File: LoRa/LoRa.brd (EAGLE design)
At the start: 59.4 x 27.9 mm, 33 parts, among them J1 UP2-AH-1-TH, U1 STM32L053C8T6, U2 RFM69HCW, U5 LM3671MF-3.3/NOPB, X1 uFL/SMA, Y1 ECS-80-S-4X

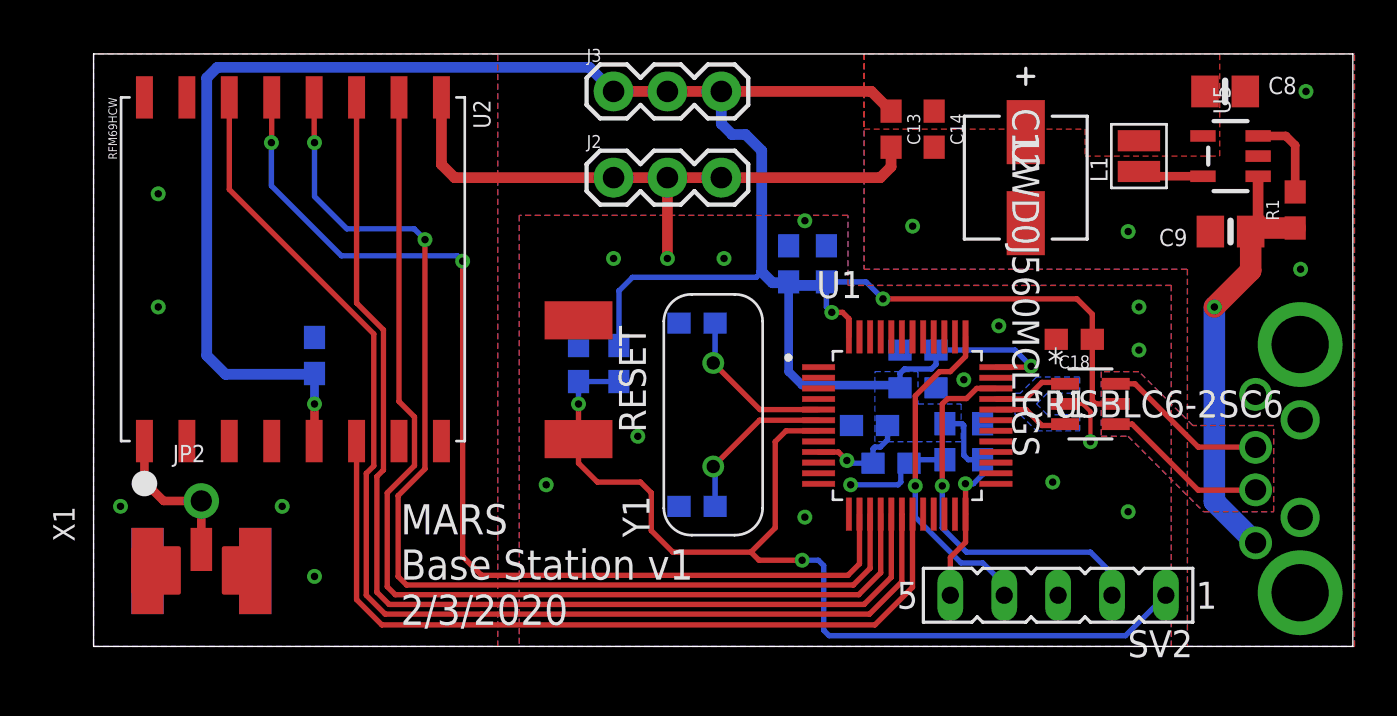
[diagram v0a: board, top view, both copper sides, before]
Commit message: LDO changes
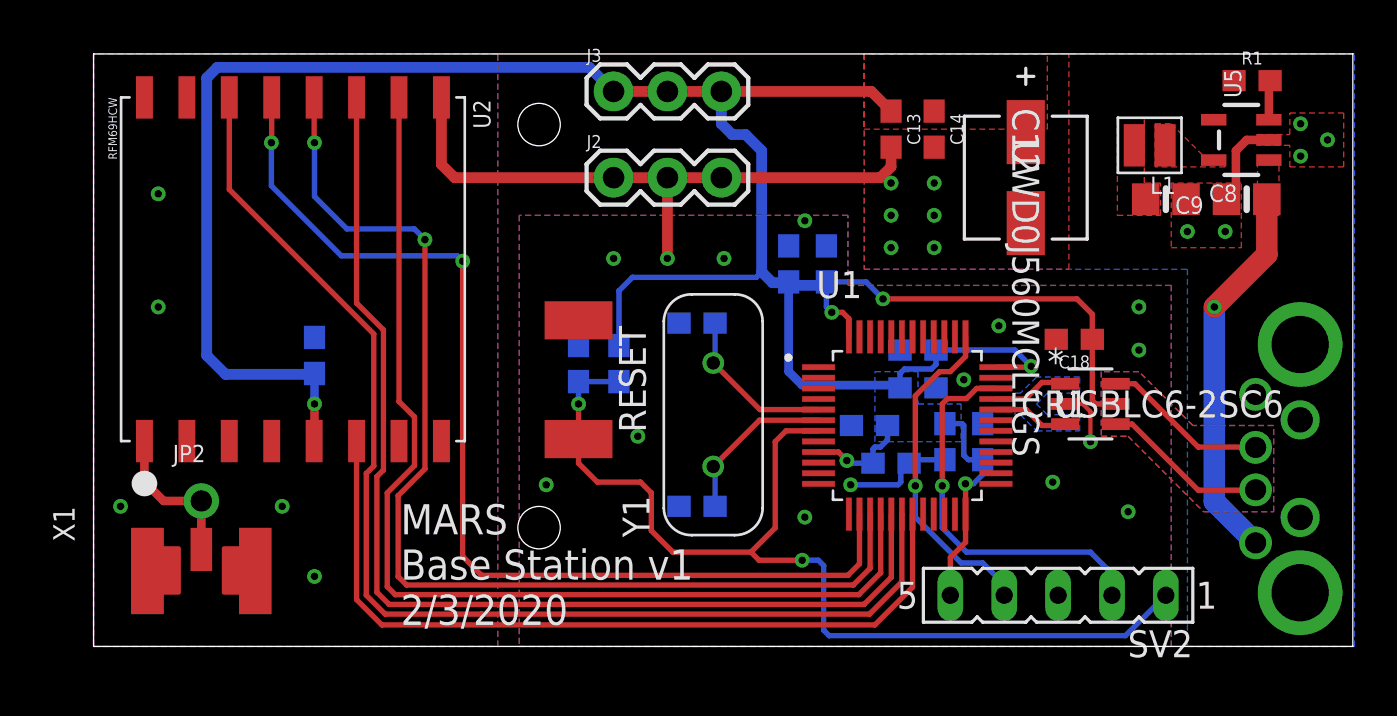
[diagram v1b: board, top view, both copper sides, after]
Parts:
- moved R1 6.43 mm to (54.6, 26.7), turned to 0 degrees
- moved C8 5.80 mm to (50.5, 21.1)
- moved C9 1.70 mm to (54.4, 21.1)
- moved U5 0.92 mm to (54.1, 23.9)
- moved L1 0.72 mm to (49.8, 23.6), turned to 180 degrees
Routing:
- net GND: track 37.5 -> 41.7 mm, vias 24 -> 31
- net 5V: track 21.4 -> 18.0 mm
- net N$2: track 3.11 -> 0.00 mm
- net EN: track 4.13 -> 1.87 mm
- added copper zone on layer 1, net 5V
- added copper zone on layer 1, net N$2
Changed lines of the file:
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@@
 <setting verticaltext="up"/>
 </settings>
-<grid distance="10" unitdist="mil" unit="mil" style="lines" multiple="1" display="yes" altdistance="5" altunitdist="mil" altunit="mil"/>
+<grid distance="0.1" unitdist="mm" unit="mm" style="lines" multiple="1" display="yes" altdistance="5" altunitdist="mil" altunit="mil"/>
 <layers>
 <layer number="1" name="Top" color="4" fill="1" visible="yes" active="yes"/>
@@
 <layer number="43" name="vRestrict" color="2" fill="10" visible="yes" active="yes"/>
 <layer number="44" name="Drills" color="7" fill="1" visible="no" active="yes"/>
-<layer number="45" name="Holes" color="7" fill="1" visible="no" active="yes"/>
+<layer number="45" name="Holes" color="7" fill="1" visible="yes" active="yes"/>
 <layer number="46" name="Milling" color="3" fill="1" visible="no" active="yes"/>
 <layer number="47" name="Measures" color="7" fill="1" visible="no" active="yes"/>
@@
 Base Station v1
 2/3/2020</text>
+<hole x="21" y="24.6" drill="2"/>
+<hole x="21" y="5.6" drill="2"/>
 </plain>
 <attributes>
@@
 <attribute name="OC_NEWARK" value="unknown" x="45.466" y="2.413" size="1.778" layer="27" rot="R180" display="off"/>
 </element>
-<element name="U5" library="microbuilder" package="SOT23-5" value="LM3671MF-3.3/NOPB" x="53.594" y="23.114" rot="R90"/>
-<element name="L1" library="microbuilder" package="INDUCTOR_TAIYOYUDEN_NRH2412T" value="2.2uH/NRH2412T2R2MNGH" x="49.276" y="23.114" rot="R90"/>
-<element name="C8" library="microbuilder" package="0805-NO" value="22uF" x="53.34" y="26.162"/>
-<element name="C9" library="microbuilder" package="0805-NO" value="10uF" x="53.594" y="19.558" rot="R180"/>
-<element name="R1" library="SparkFun-Resistors" library_urn="urn:adsk.eagle:library:532" package="0603" package3d_urn="urn:adsk.eagle:package:39650/1" value="100k" x="56.642" y="20.574" rot="R90">
-<attribute name="PROD_ID" value="RES-07828" x="56.642" y="20.574" size="1.778" layer="27" rot="R90" display="off"/>
+<element name="U5" library="microbuilder" package="SOT23-5" value="LM3671MF-3.3/NOPB" x="54.102" y="23.876" rot="R90"/>
+<element name="L1" library="microbuilder" package="INDUCTOR_TAIYOYUDEN_NRH2412T" value="2.2uH/NRH2412T2R2MNGH" x="49.784" y="23.622" rot="R180"/>
+<element name="C8" library="microbuilder" package="0805-NO" value="22uF" x="50.546" y="21.082"/>
+<element name="C9" library="microbuilder" package="0805-NO" value="10uF" x="54.356" y="21.082" rot="R180"/>
+<element name="R1" library="SparkFun-Resistors" library_urn="urn:adsk.eagle:library:532" package="0603" package3d_urn="urn:adsk.eagle:package:39650/1" value="100k" x="54.61" y="26.67">
+<attribute name="PROD_ID" value="RES-07828" x="54.61" y="26.67" size="1.778" layer="27" display="off"/>
 </element>
 <element name="C10" library="SparkFun-Capacitors" library_urn="urn:adsk.eagle:library:510" package="0603" package3d_urn="urn:adsk.eagle:package:37414/1" value="20pF" x="28.448" y="6.604" rot="MR0">
@@
 <contactref element="C13" pad="2"/>
 <contactref element="C14" pad="2"/>
-<polygon width="0.2032" layer="1" rank="4">
-<vertex x="36.322" y="27.94"/>
-<vertex x="36.322" y="17.78"/>
-<vertex x="51.562" y="17.78"/>
-<vertex x="51.562" y="0"/>
-<vertex x="59.436" y="0"/>
-<vertex x="59.436" y="27.94"/>
-</polygon>
 <contactref element="C15" pad="2"/>
 <contactref element="C16" pad="2"/>
@@
 <via x="3.048" y="21.336" extent="1-16" drill="0.35"/>
 <via x="3.048" y="16.002" extent="1-16" drill="0.35"/>
-<via x="38.608" y="19.812" extent="1-16" drill="0.35"/>
-<via x="48.768" y="19.558" extent="1-16" drill="0.35"/>
-<via x="57.15" y="26.162" extent="1-16" drill="0.35"/>
-<via x="56.896" y="17.78" extent="1-16" drill="0.35"/>
+<via x="37.592" y="20.32" extent="1-16" drill="0.35"/>
 <via x="48.768" y="6.35" extent="1-16" drill="0.35"/>
 <via x="33.528" y="6.096" extent="1-16" drill="0.35"/>
+<polygon width="0.2032" layer="1" rank="4">
+<vertex x="36.322" y="27.94"/>
+<vertex x="36.322" y="17.78"/>
+<vertex x="45.974" y="17.78"/>
+<vertex x="45.974" y="27.94"/>
+</polygon>
+<via x="37.592" y="21.844" extent="1-16" drill="0.35"/>
+<via x="39.624" y="21.844" extent="1-16" drill="0.35"/>
+<polygon width="0.2032" layer="1" thermals="no">
+<vertex x="50.8" y="21.844"/>
+<vertex x="50.8" y="18.796"/>
+<vertex x="54.102" y="18.796"/>
+<vertex x="54.102" y="21.844"/>
+</polygon>
+<via x="51.562" y="19.558" extent="1-16" drill="0.35"/>
+<via x="53.34" y="19.558" extent="1-16" drill="0.35"/>
+<wire x1="55.4021" y1="23.876" x2="54.356" y2="23.876" width="0.4064" layer="1"/>
+<wire x1="53.848" y1="21.524" x2="53.406" y2="21.082" width="0.4064" layer="1"/>
+<wire x1="54.356" y1="23.876" x2="53.848" y2="23.368" width="0.4064" layer="1"/>
+<wire x1="53.848" y1="23.368" x2="53.848" y2="21.524" width="0.4064" layer="1"/>
+<polygon width="0.2032" layer="1" thermals="no">
+<vertex x="54.864" y="24.13"/>
+<vertex x="56.388" y="24.13"/>
+<vertex x="56.388" y="25.146"/>
+<vertex x="58.928" y="25.146"/>
+<vertex x="58.928" y="22.606"/>
+<vertex x="56.388" y="22.606"/>
+<vertex x="56.388" y="23.622"/>
+<vertex x="54.864" y="23.622"/>
+</polygon>
+<via x="56.896" y="24.638" extent="1-16" drill="0.35"/>
+<via x="58.166" y="23.876" extent="1-16" drill="0.35"/>
+<via x="56.896" y="23.114" extent="1-16" drill="0.35"/>
+<via x="37.592" y="18.796" extent="1-16" drill="0.35"/>
+<via x="39.624" y="18.796" extent="1-16" drill="0.35"/>
+<via x="39.624" y="20.32" extent="1-16" drill="0.35"/>
 </signal>
 <signal name="3.3V">
@@
 <contactref element="C13" pad="1"/>
 <contactref element="C14" pad="1"/>
-<wire x1="49.501" y1="24.064" x2="49.276" y2="23.839" width="0.4064" layer="1"/>
-<polygon width="0.2032" layer="1">
-<vertex x="36.322" y="27.94"/>
-<vertex x="36.322" y="24.384"/>
-<vertex x="46.736" y="24.384"/>
-<vertex x="46.736" y="23.114"/>
-<vertex x="53.086" y="23.114"/>
-<vertex x="53.086" y="27.94"/>
-</polygon>
 <contactref element="C15" pad="1"/>
 <contactref element="C16" pad="1"/>
@@
 <wire x1="47.078" y1="15.66" x2="47.078" y2="14.478" width="0.254" layer="1"/>
 <wire x1="46.355" y1="16.383" x2="47.078" y2="15.66" width="0.254" layer="1"/>
+<polygon width="0.2032" layer="1" thermals="no">
+<vertex x="36.322" y="27.94"/>
+<vertex x="36.322" y="24.384"/>
+<vertex x="44.958" y="24.384"/>
+<vertex x="44.958" y="27.94"/>
+</polygon>
+<polygon width="0.2032" layer="1" thermals="no">
+<vertex x="48.26" y="24.892"/>
+<vertex x="48.26" y="20.32"/>
+<vertex x="50.292" y="20.32"/>
+<vertex x="50.292" y="21.844"/>
+<vertex x="49.53" y="21.844"/>
+<vertex x="49.53" y="24.892"/>
+</polygon>
+<wire x1="49.059" y1="23.622" x2="52.8019" y2="24.826" width="0" layer="19" extent="1-1"/>
+<wire x1="43.942" y1="24.2443" x2="49.059" y2="23.622" width="0" layer="19" extent="1-1"/>
 </signal>
 <signal name="RST">
@@
 <contactref element="C9" pad="1"/>
 <contactref element="R1" pad="1"/>
-<wire x1="54.8941" y1="22.164" x2="54.8941" y2="19.558" width="0.508" layer="1"/>
-<wire x1="54.8941" y1="19.558" x2="54.544" y2="19.558" width="0.508" layer="1"/>
-<wire x1="54.544" y1="19.558" x2="54.544" y2="19.724" width="1.016" layer="1"/>
-<wire x1="54.544" y1="19.724" x2="56.642" y2="19.724" width="1.016" layer="1"/>
 <wire x1="54.776" y1="4.882" x2="52.832" y2="6.826" width="1.016" layer="16"/>
 <wire x1="52.832" y1="6.826" x2="52.832" y2="16.002" width="1.016" layer="16"/>
 <via x="52.832" y="16.002" extent="1-16" drill="0.35"/>
-<wire x1="52.832" y1="16.002" x2="54.544" y2="17.714" width="1.016" layer="1"/>
-<wire x1="54.544" y1="17.714" x2="54.544" y2="19.558" width="1.016" layer="1"/>
+<polygon width="0.2032" layer="1" thermals="no">
+<vertex x="54.864" y="20.32"/>
+<vertex x="54.864" y="23.114"/>
+<vertex x="55.88" y="23.114"/>
+<vertex x="55.88" y="20.32"/>
+</polygon>
+<wire x1="55.306" y1="21.082" x2="55.306" y2="18.476" width="1.016" layer="1"/>
+<wire x1="55.306" y1="18.476" x2="52.832" y2="16.002" width="1.016" layer="1"/>
+<wire x1="55.4021" y1="22.926" x2="53.76" y2="26.67" width="0" layer="19" extent="1-1"/>
 </signal>
 <signal name="SPI1_SCK">
@@
 <contactref element="L1" pad="1"/>
 <contactref element="U5" pad="5"/>
-<wire x1="52.2939" y1="22.164" x2="49.501" y2="22.164" width="0.4064" layer="1"/>
-<wire x1="49.501" y1="22.164" x2="49.276" y2="22.389" width="0.4064" layer="1"/>
+<polygon width="0.2032" layer="1" thermals="no">
+<vertex x="53.34" y="22.606"/>
+<vertex x="50.038" y="22.606"/>
+<vertex x="50.038" y="24.638"/>
+<vertex x="50.8" y="24.638"/>
+<vertex x="52.324" y="23.114"/>
+<vertex x="53.34" y="23.114"/>
+</polygon>
 </signal>
 <signal name="EN">
 <contactref element="U5" pad="3"/>
 <contactref element="R1" pad="2"/>
-<wire x1="54.8941" y1="24.064" x2="56.2" y2="24.064" width="0.4064" layer="1"/>
-<wire x1="56.2" y1="24.064" x2="56.642" y2="23.622" width="0.4064" layer="1"/>
-<wire x1="56.642" y1="23.622" x2="56.642" y2="21.424" width="0.4064" layer="1"/>
+<wire x1="55.4021" y1="24.826" x2="55.4021" y2="26.6121" width="0.4064" layer="1"/>
+<wire x1="55.4021" y1="26.6121" x2="55.46" y2="26.67" width="0.4064" layer="1"/>
 </signal>
 <signal name="OSC_OUT">

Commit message: This board is a work of art
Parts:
- moved R1 1.68 mm to (56.3, 26.6), turned to 180 degrees
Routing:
- net 3.3V: track 134.7 -> 144.9 mm
- net 5V: track 18.0 -> 28.1 mm
- net GND: vias 31 -> 32
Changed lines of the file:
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@@
 <setting verticaltext="up"/>
 </settings>
-<grid distance="0.1" unitdist="mm" unit="mm" style="lines" multiple="1" display="yes" altdistance="5" altunitdist="mil" altunit="mil"/>
+<grid distance="10" unitdist="mil" unit="mil" style="lines" multiple="1" display="yes" altdistance="5" altunitdist="mil" altunit="mil"/>
 <layers>
 <layer number="1" name="Top" color="4" fill="1" visible="yes" active="yes"/>
@@
 <element name="C8" library="microbuilder" package="0805-NO" value="22uF" x="50.546" y="21.082"/>
 <element name="C9" library="microbuilder" package="0805-NO" value="10uF" x="54.356" y="21.082" rot="R180"/>
-<element name="R1" library="SparkFun-Resistors" library_urn="urn:adsk.eagle:library:532" package="0603" package3d_urn="urn:adsk.eagle:package:39650/1" value="100k" x="54.61" y="26.67">
-<attribute name="PROD_ID" value="RES-07828" x="54.61" y="26.67" size="1.778" layer="27" display="off"/>
+<element name="R1" library="SparkFun-Resistors" library_urn="urn:adsk.eagle:library:532" package="0603" package3d_urn="urn:adsk.eagle:package:39650/1" value="100k" x="56.29" y="26.63" rot="R180">
+<attribute name="PROD_ID" value="RES-07828" x="56.29" y="26.63" size="1.778" layer="27" rot="R180" display="off"/>
 </element>
 <element name="C10" library="SparkFun-Capacitors" library_urn="urn:adsk.eagle:library:510" package="0603" package3d_urn="urn:adsk.eagle:package:37414/1" value="20pF" x="28.448" y="6.604" rot="MR0">
@@
 <vertex x="36.322" y="17.78"/>
 <vertex x="51.562" y="17.78"/>
-<vertex x="51.562" y="0"/>
-<vertex x="59.436" y="0"/>
+<vertex x="51.562" y="10.668"/>
+<vertex x="59.436" y="10.668"/>
 <vertex x="59.436" y="27.94"/>
 <vertex x="36.322" y="27.94"/>
@@
 <vertex x="54.102" y="21.844"/>
 </polygon>
-<via x="51.562" y="19.558" extent="1-16" drill="0.35"/>
-<via x="53.34" y="19.558" extent="1-16" drill="0.35"/>
+<via x="51.181" y="19.558" extent="1-16" drill="0.35"/>
+<via x="53.721" y="19.558" extent="1-16" drill="0.35"/>
 <wire x1="55.4021" y1="23.876" x2="54.356" y2="23.876" width="0.4064" layer="1"/>
 <wire x1="53.848" y1="21.524" x2="53.406" y2="21.082" width="0.4064" layer="1"/>
@@
 <vertex x="56.388" y="24.13"/>
 <vertex x="56.388" y="25.146"/>
-<vertex x="58.928" y="25.146"/>
-<vertex x="58.928" y="22.606"/>
+<vertex x="58.293" y="25.146"/>
+<vertex x="58.293" y="22.606"/>
 <vertex x="56.388" y="22.606"/>
 <vertex x="56.388" y="23.622"/>
@@
 </polygon>
 <via x="56.896" y="24.638" extent="1-16" drill="0.35"/>
-<via x="58.166" y="23.876" extent="1-16" drill="0.35"/>
+<via x="57.785" y="23.876" extent="1-16" drill="0.35"/>
 <via x="56.896" y="23.114" extent="1-16" drill="0.35"/>
 <via x="37.592" y="18.796" extent="1-16" drill="0.35"/>
 <via x="39.624" y="18.796" extent="1-16" drill="0.35"/>
 <via x="39.624" y="20.32" extent="1-16" drill="0.35"/>
+<via x="52.451" y="19.558" extent="1-16" drill="0.35"/>
 </signal>
 <signal name="3.3V">
@@
 <vertex x="49.53" y="24.892"/>
 </polygon>
+<wire x1="49.596" y1="21.082" x2="47.7393" y2="21.082" width="1.016" layer="1"/>
+<wire x1="47.7393" y1="21.082" x2="47.2313" y2="21.59" width="1.016" layer="1"/>
+<wire x1="47.2313" y1="25.0450875" x2="46.8890875" y2="25.3873" width="1.016" layer="1"/>
+<wire x1="44.6525125" y1="25.3873" x2="44.3103" y2="25.0450875" width="1.016" layer="1"/>
+<wire x1="47.2313" y1="21.59" x2="47.2313" y2="25.0450875" width="1.016" layer="1"/>
+<wire x1="46.8890875" y1="25.3873" x2="44.6525125" y2="25.3873" width="1.016" layer="1"/>
+<wire x1="44.3103" y1="25.0450875" x2="44.3103" y2="24.6126" width="1.016" layer="1"/>
+<wire x1="44.3103" y1="24.6126" x2="43.942" y2="24.2443" width="1.016" layer="1"/>
 <wire x1="49.059" y1="23.622" x2="52.8019" y2="24.826" width="0" layer="19" extent="1-1"/>
-<wire x1="43.942" y1="24.2443" x2="49.059" y2="23.622" width="0" layer="19" extent="1-1"/>
 </signal>
 <signal name="RST">
@@
 <wire x1="55.306" y1="21.082" x2="55.306" y2="18.476" width="1.016" layer="1"/>
 <wire x1="55.306" y1="18.476" x2="52.832" y2="16.002" width="1.016" layer="1"/>
-<wire x1="55.4021" y1="22.926" x2="53.76" y2="26.67" width="0" layer="19" extent="1-1"/>
+<wire x1="57.14" y1="26.63" x2="58.4348" y2="26.63" width="0.4064" layer="1"/>
+<wire x1="58.4348" y1="26.63" x2="58.7758" y2="26.289" width="0.4064" layer="1"/>
+<wire x1="58.7758" y1="26.289" x2="58.7758" y2="21.6918" width="0.4064" layer="1"/>
+<wire x1="58.7758" y1="21.6918" x2="58.166" y2="21.082" width="0.4064" layer="1"/>
+<wire x1="58.166" y1="21.082" x2="55.306" y2="21.082" width="0.4064" layer="1"/>
 </signal>
 <signal name="SPI1_SCK">
@@
 <contactref element="U5" pad="3"/>
 <contactref element="R1" pad="2"/>
-<wire x1="55.4021" y1="24.826" x2="55.4021" y2="26.6121" width="0.4064" layer="1"/>
-<wire x1="55.4021" y1="26.6121" x2="55.46" y2="26.67" width="0.4064" layer="1"/>
+<wire x1="55.4021" y1="24.826" x2="55.4021" y2="26.5921" width="0.4064" layer="1"/>
+<wire x1="55.4021" y1="26.5921" x2="55.44" y2="26.63" width="0.4064" layer="1"/>
 </signal>
 <signal name="OSC_OUT">
